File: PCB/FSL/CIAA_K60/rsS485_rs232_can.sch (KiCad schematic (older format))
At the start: 45 parts, among them J401 RS485, J402 DB9, J403 CAN, U401 SP1486EEN-L, U402 ST3232E, U403 AMIS42665TJAA1RG

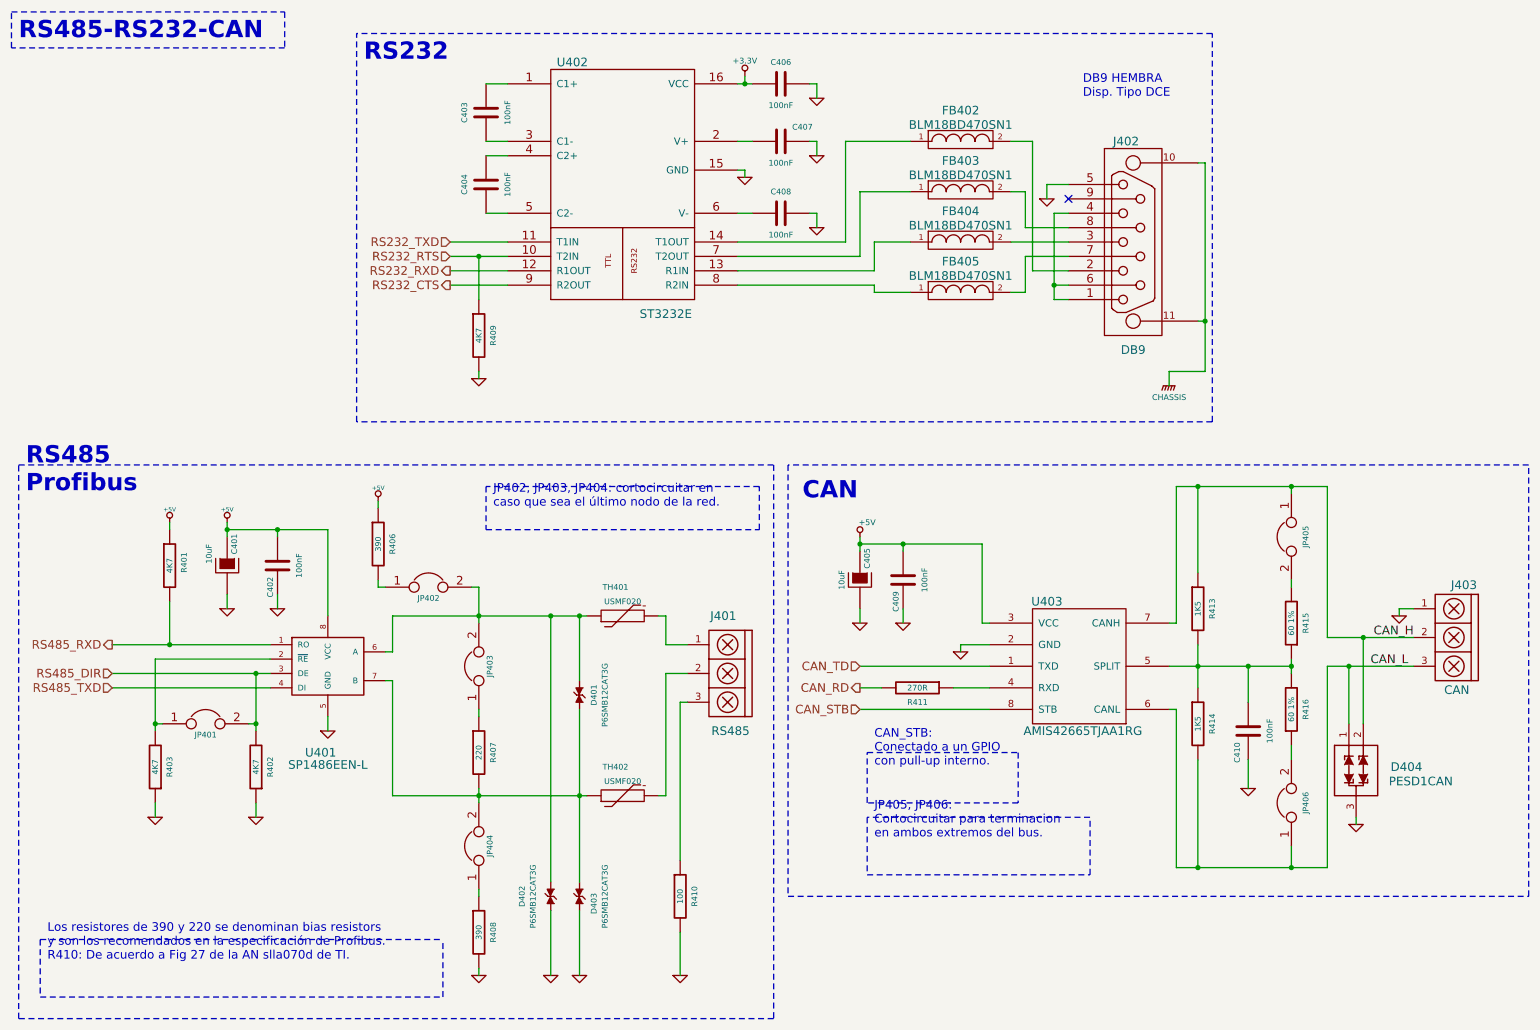
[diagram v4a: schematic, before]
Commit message: Sch files adapted to new eeschema. Fixing some text locations.
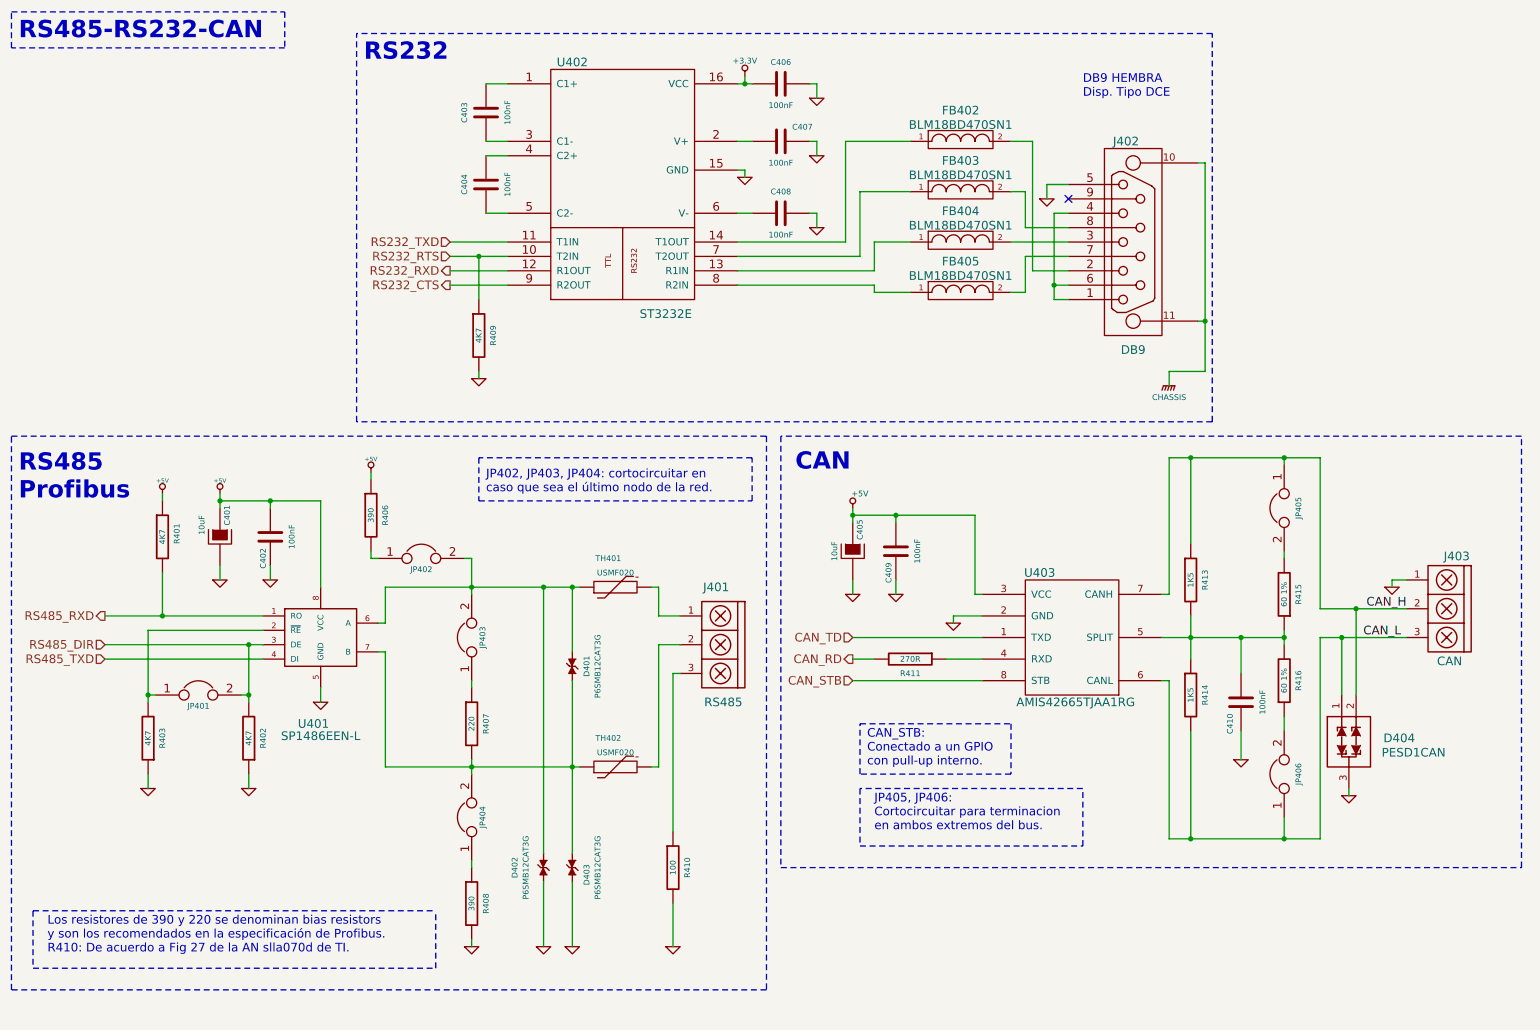
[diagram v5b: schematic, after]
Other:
- moved on the sheet: C401, C402, C405, C409, C410, D401, D402, D403, D404, J401, J403, JP401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

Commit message: Renaming symbol field-names in .sch files for KiCost integration.
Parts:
- C401, C405: Desc (none) -> CAP TANT 10UF 6.3V 10% 1206; Descripcion CAP TANT 10UF 6.3V 10% 1206 -> (none); Digikey# (none) -> 399-10116-1-ND; Digikey/Mouser 399-10116-1-ND -> (none); Fabricante Kemet -> (none); Manf (none) -> Kemet; Manf# (none) -> T491A106K006AT7280; Nro. parte T491A106K006AT7280 -> (none)
- C402, C403, C404, C406, C407, C408, C409, C410: Desc (none) -> CAP CER 0.1UF 16V 10% X7R 0603; Descripcion CAP CER 0.1UF 16V 10% X7R 0603 -> (none); Digikey# (none) -> 399-1096-1-ND; Digikey/Mouser 399-1096-1-ND -> (none); Fabricante Kemet -> (none); Manf (none) -> Kemet; Manf# (none) -> C0603C104K4RACTU; Nro. parte C0603C104K4RACTU -> (none)
- D401, D402, D403: Desc (none) -> TVS DIODE 10.2VWM 16.7VC SMB; Descripcion TVS DIODE 10.2VWM 16.7VC SMB -> (none); Digikey# (none) -> P6SMB12CAT3GOSCT-ND; Digikey/Mouser P6SMB12CAT3GOSCT-ND -> (none); Fabricante ON Semiconductor -> (none); Manf (none) -> ON Semiconductor; Manf# (none) -> P6SMB12CAT3G; Nro. parte P6SMB12CAT3G -> (none)
- D404: Desc (none) -> TVS DIODE 24VWM 70VC SOT23; Descripcion TVS DIODE 24VWM 70VC SOT23 -> (none); Digikey# (none) -> 568-4032-1-ND; Digikey/Mouser 568-4032-1-ND -> (none); Fabricante NXP Semiconductors -> (none); Manf (none) -> NXP Semiconductors; Manf# (none) -> PESD1CAN,215; Nro. parte PESD1CAN,215 -> (none)
- FB402, FB403, FB404, FB405: Desc (none) -> FERRITE CHIP 47 OHM 500MA 0603; Descripcion FERRITE CHIP 47 OHM 500MA 0603 -> (none); Digikey# (none) -> 490-5211-1-ND; Digikey/Mouser 490-5211-1-ND -> (none); Fabricante Murata Electronics North America -> (none); Manf (none) -> Murata Electronics North America; Manf# (none) -> BLM18BD470SN1D; Nro. parte BLM18BD470SN1D -> (none)
- J401, J403: Desc (none) -> TERM BLOCK 5.08MM VERT 3POS PCB; Descripcion TERM BLOCK 5.08MM VERT 3POS PCB -> (none); Digikey# (none) -> 571-7969493; Digikey/Mouser 571-7969493 -> (none); Fabricante TE Connectivity -> (none); Manf (none) -> TE Connectivity; Manf# (none) -> 796949-3; Nro. parte 796949-3 -> (none)
- J402: Desc (none) -> CONN D-SUB RCPT 9POS RA GOLD; Descripcion CONN D-SUB RCPT 9POS RA GOLD -> (none); Digikey# (none) -> S9554-ND; Digikey/Mouser S9554-ND -> (none); Fabricante Sullins -> (none); Manf (none) -> Sullins; Manf# (none) -> SDS107-PRP1-F09-SN63-11; Nro. parte SDS107-PRP1-F09-SN63-11 -> (none)
- JP401, JP402, JP403, JP404, JP405, JP406: Desc (none) -> JUMPER 2 TERM; Descripcion JUMPER 2 TERM -> (none); Digikey# (none) -> S1212EC-40-ND; Digikey/Mouser S1212EC-40-ND -> (none); Fabricante Sullins Connector Solutions -> (none); Manf (none) -> Sullins Connector Solutions; Manf# (none) -> PREC040SFAN-RC; Nro. parte PREC040SFAN-RC -> (none)
- R401, R402, R403, R409: Desc (none) -> RES 4.7K OHM 1/10W 5% 0603 SMD; Descripcion RES 4.7K OHM 1/10W 5% 0603 SMD -> (none); Digikey# (none) -> 311-4.7KGRCT-ND; Digikey/Mouser 311-4.7KGRCT-ND -> (none); Fabricante Yageo -> (none); Manf (none) -> Yageo; Manf# (none) -> RC0603JR-074K7L; Nro. parte RC0603JR-074K7L -> (none)
- R406, R408: Desc (none) -> RES 390 OHM 1/10W 5% 0603 SMD; Descripcion RES 390 OHM 1/10W 5% 0603 SMD -> (none); Digikey# (none) -> 311-390GRCT-ND; Digikey/Mouser 311-390GRCT-ND -> (none); Fabricante Yageo -> (none); Manf (none) -> Yageo; Manf# (none) -> RC0603JR-07390RL; Nro. parte RC0603JR-07390RL -> (none)
- R407: Desc (none) -> RES 220 OHM 1/10W 5% 0603 SMD; Descripcion RES 220 OHM 1/10W 5% 0603 SMD -> (none); Digikey# (none) -> 311-220GRCT-ND; Digikey/Mouser 311-220GRCT-ND -> (none); Fabricante Yageo -> (none); Manf (none) -> Yageo; Manf# (none) -> RC0603JR-07220RL; Nro. parte RC0603JR-07220RL -> (none)
- R410: Desc (none) -> RES 100 OHM 1/2W 5% 2010 SMD; Descripcion RES 100 OHM 1/2W 5% 2010 SMD -> (none); Digikey# (none) -> CR2010-JW-101ELFCT-ND; Digikey/Mouser CR2010-JW-101ELFCT-ND -> (none); Fabricante Bourns Inc. -> (none); Manf (none) -> Bourns; Manf# (none) -> CR2010-JW-101ELF; Nro. parte CR2010-JW-101ELF -> (none)
- R411: Desc (none) -> RES 270 OHM 1/10W 5% 0603 SMD; Descripcion RES 270 OHM 1/10W 5% 0603 SMD -> (none); Digikey# (none) -> 311-270GRCT-ND; Digikey/Mouser 311-270GRCT-ND -> (none); Fabricante Yageo -> (none); Manf (none) -> Yageo; Manf# (none) -> RC0603JR-07270RL; Nro. parte RC0603JR-07270RL -> (none)
- R413, R414: Desc (none) -> RES 1.5K OHM 1/10W 5% 0603 SMD; Descripcion RES 1.5K OHM 1/10W 5% 0603 SMD -> (none); Digikey# (none) -> 311-1.5KGRCT-ND; Digikey/Mouser 311-1.5KGRCT-ND -> (none); Fabricante Yageo -> (none); Manf (none) -> Yageo; Manf# (none) -> RC0603JR-071K5L; Nro. parte RC0603JR-071K5L -> (none)
- R415, R416: Desc (none) -> RES 59.0 OHM 1/10W 1% 0603 SMD; Descripcion RES 59.0 OHM 1/10W 1% 0603 SMD -> (none); Digikey# (none) -> 311-59.0HRCT-ND; Digikey/Mouser 311-59.0HRCT-ND -> (none); Fabricante Yageo -> (none); Manf (none) -> Yageo; Manf# (none) -> RC0603FR-0759RL; Nro. parte RC0603FR-0759RL -> (none)
- TH401, TH402: Desc (none) -> FUSE RESETTABLE .20A 30V HLD SMD; Descripcion FUSE RESETTABLE .20A 30V HLD SMD -> (none); Digikey# (none) -> MF-USMF020-2CT-ND; Digikey/Mouser MF-USMF020-2CT-ND -> (none); Fabricante Bourns Inc. -> (none); Manf (none) -> Bourns; Manf# (none) -> MF-USMF020-2; Nro. parte MF-USMF020-2 -> (none)
- U401: Desc (none) -> IC TXRX RS485/422 PROFIBUS 8SOIC; Descripcion IC TXRX RS485/422 PROFIBUS 8SOIC -> (none); Digikey# (none) -> 1016-1003-5-ND; Digikey/Mouser 1016-1003-5-ND -> (none); Fabricante Exar Corporation -> (none); Manf (none) -> Exar Corporation; Manf# (none) -> SP1486EEN-L; Nro. parte SP1486EEN-L -> (none)
- U402: Desc (none) -> IC DRVR/RCVR RS232 ESD 16-TSSOP; Descripcion IC DRVR/RCVR RS232 ESD 16-TSSOP -> (none); Digikey# (none) -> 497-6538-1-ND; Digikey/Mouser 497-6538-1-ND -> (none); Fabricante STMicroelectronics -> (none); Manf (none) -> STMicroelectronics; Manf# (none) -> ST3232ECTR; Nro. parte ST3232ECTR -> (none)
- U403: Desc (none) -> TRANSCEIVER CAN HS LO PWR 8-SOIC; Descripcion TRANSCEIVER CAN HS LO PWR 8-SOIC -> (none); Digikey# (none) -> 766-1006-1-ND; Digikey/Mouser 766-1006-1-ND -> (none); Fabricante ON Semiconductor -> (none); Manf (none) -> ON Semiconductor; Manf# (none) -> AMIS42665TJAA1RG; Nro. parte AMIS42665TJAA1RG -> (none)
